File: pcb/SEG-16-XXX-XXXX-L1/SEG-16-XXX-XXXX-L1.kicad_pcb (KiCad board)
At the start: 2 copper layers, 66.7 x 100 mm, 23 parts, among them U1 STM8S003, U2 TM1640

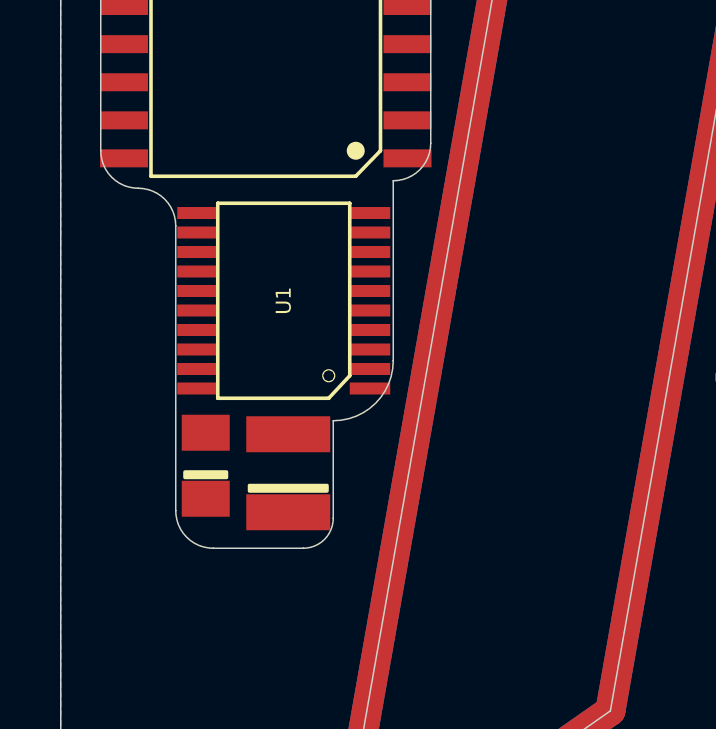
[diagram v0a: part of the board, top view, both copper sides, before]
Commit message: Updated to 0V6 changed images
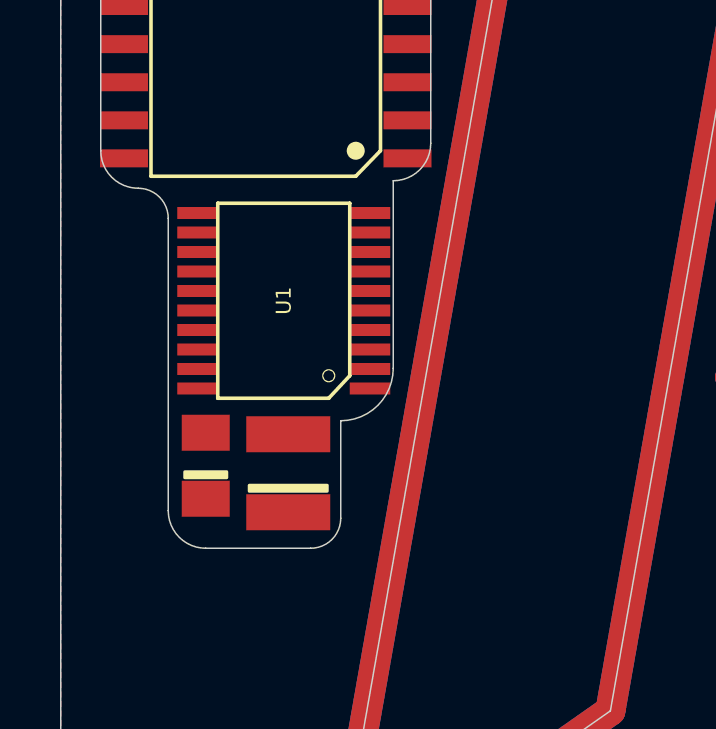
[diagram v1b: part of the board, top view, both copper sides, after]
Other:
- outline, holes or cut-outs redrawn
- board text added: "0V6"
- board text removed: "0V5"
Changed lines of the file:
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@@
     (effects (font (size 1 1) (thickness 0.15)) (justify mirror))
   )
-  (gr_text 0V5 (at 26 30) (layer B.SilkS)
+  (gr_text 0V6 (at 26 30) (layer B.SilkS)
     (effects (font (size 1.5 1.5) (thickness 0.3)) (justify mirror))
   )
@@
   (gr_line (start -5 -50) (end 5 -50) (layer Edge.Cuts) (width 0.05))
   (gr_line (start -7.5 -47.5) (end -5 -50) (layer Edge.Cuts) (width 0.05))
-  (gr_arc (start -25.25 -13.25) (end -25.25 -12.25) (angle -90) (layer Edge.Cuts) (width 0.05))
-  (gr_arc (start -28.25 -13.5) (end -29.5 -13.5) (angle -90) (layer Edge.Cuts) (width 0.05))
+  (gr_arc (start -25 -13.25) (end -25 -12.25) (angle -90) (layer Edge.Cuts) (width 0.05))
+  (gr_arc (start -28.5 -13.5) (end -29.75 -13.5) (angle -90) (layer Edge.Cuts) (width 0.05))
   (gr_arc (start -14.5 -41.75) (end -14.5 -40.5) (angle -90) (layer Edge.Cuts) (width 0.05))
   (gr_arc (start -17 -41.75) (end -18.25 -41.75) (angle -90) (layer Edge.Cuts) (width 0.05))
   (gr_arc (start -17 -42.25) (end -17 -43.5) (angle -90) (layer Edge.Cuts) (width 0.05))
   (gr_arc (start -14.5 -42.25) (end -13.25 -42.25) (angle -90) (layer Edge.Cuts) (width 0.05))
-  (gr_arc (start -30.75 -23) (end -29.5 -23) (angle -90) (layer Edge.Cuts) (width 0.05))
+  (gr_arc (start -30.75 -23.25) (end -29.75 -23.25) (angle -90) (layer Edge.Cuts) (width 0.05))
   (gr_arc (start -30.75 -25.5) (end -32 -25.5) (angle -90) (layer Edge.Cuts) (width 0.05))
   (gr_arc (start -30.75 -41.5) (end -30.75 -42.75) (angle -90) (layer Edge.Cuts) (width 0.05))
   (gr_arc (start -22.25 -41.5) (end -21 -41.5) (angle -90) (layer Edge.Cuts) (width 0.05))
   (gr_arc (start -22.25 -25.75) (end -22.25 -24.5) (angle -90) (layer Edge.Cuts) (width 0.05))
-  (gr_arc (start -24.25 -18.5) (end -24.25 -16.5) (angle -90) (layer Edge.Cuts) (width 0.05))
+  (gr_arc (start -24 -18.25) (end -24 -16.5) (angle -90) (layer Edge.Cuts) (width 0.05))
   (gr_line (start 24.4383 31.9587) (end 27.7495 31.9587) (layer Edge.Cuts) (width 0.05))
   (gr_line (start 27.7495 31.9587) (end 30.0951 34.2973) (layer Edge.Cuts) (width 0.05))
@@
   (gr_line (start -17 -40.5) (end -14.5 -40.5) (layer Edge.Cuts) (width 0.05))
   (gr_line (start -18.25 -42.25) (end -18.25 -41.75) (layer Edge.Cuts) (width 0.05))
-  (gr_line (start -28.25 -12.25) (end -25.25 -12.25) (layer Edge.Cuts) (width 0.05))
-  (gr_line (start -24.25 -13.25) (end -24.25 -16.5) (layer Edge.Cuts) (width 0.05))
+  (gr_line (start -28.5 -12.25) (end -25 -12.25) (layer Edge.Cuts) (width 0.05))
+  (gr_line (start -24 -13.25) (end -24 -16.5) (layer Edge.Cuts) (width 0.05))
   (gr_line (start -22.25 -42.75) (end -30.75 -42.75) (layer Edge.Cuts) (width 0.05))
   (gr_line (start -21 -25.75) (end -21 -41.5) (layer Edge.Cuts) (width 0.05))
-  (gr_line (start -22.25 -18.5) (end -22.25 -24.5) (layer Edge.Cuts) (width 0.05))
-  (gr_line (start -29.5 -23) (end -29.5 -13.5) (layer Edge.Cuts) (width 0.05))
+  (gr_line (start -22.25 -18.25) (end -22.25 -24.5) (layer Edge.Cuts) (width 0.05))
+  (gr_line (start -29.75 -23.25) (end -29.75 -13.5) (layer Edge.Cuts) (width 0.05))
   (gr_line (start -32 -41.5) (end -32 -25.5) (layer Edge.Cuts) (width 0.05))
   (gr_line (start -5.6086 5.955) (end -9.2865 17.9565) (layer F.Cu) (width 1))
